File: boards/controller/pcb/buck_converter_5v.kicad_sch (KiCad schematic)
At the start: 10 parts, among them U801 LMR51430YFDDCR

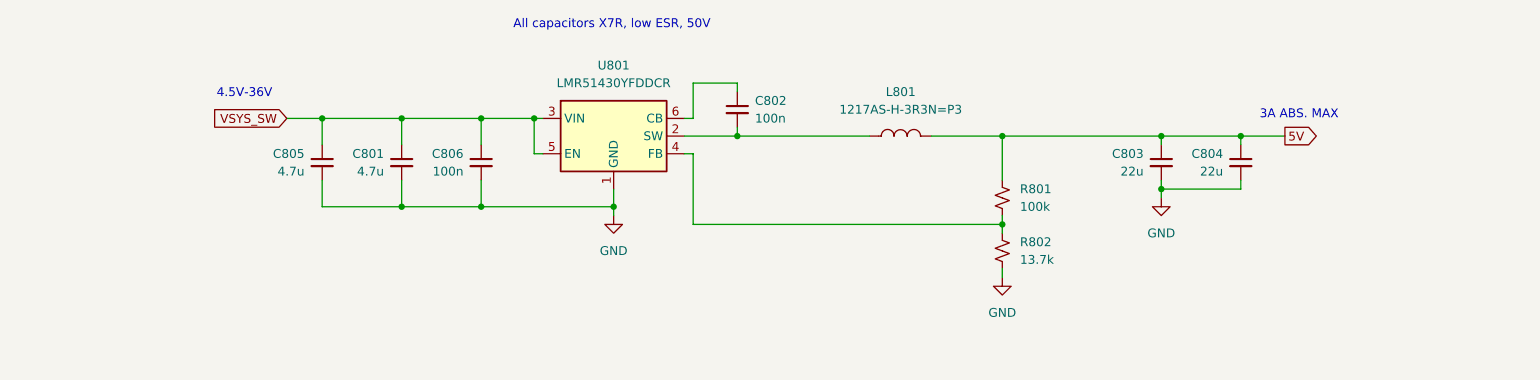
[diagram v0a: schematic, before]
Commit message: controller: pcb: Update schematic
Signed-off-by: Nicholas Loehrke <nicholasnloehrke@gmail.com>
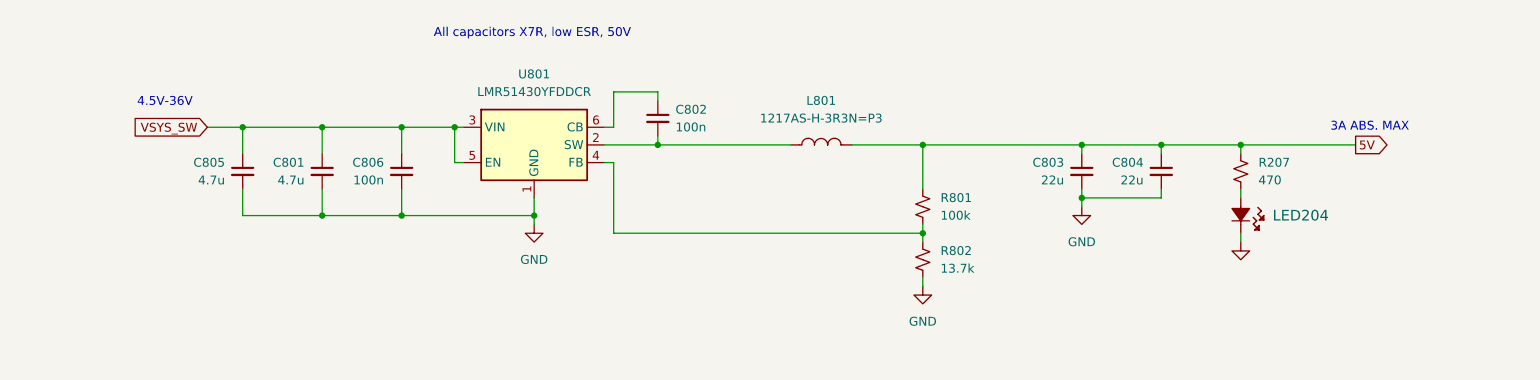
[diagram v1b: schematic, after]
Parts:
- added LED204: B1911PG--20D000514U1930, LED_B1911PG--20D000514U1930_HVK, symbol B1911PG--20D000514U1930:B1911PG--20D000514U1930
- added R207: 470, symbol Device:R_Small_US
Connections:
- net 5V: now also R207.1
- net GND: now also LED204.1
- new net: LED204.2, R207.2
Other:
- moved on the sheet: C801, C802, C803, C804, C805, C806, L801, R801, R802, U801

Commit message: controller: pcb: Update schematic
Signed-off-by: Nicholas Loehrke <nicholasnloehrke@gmail.com>
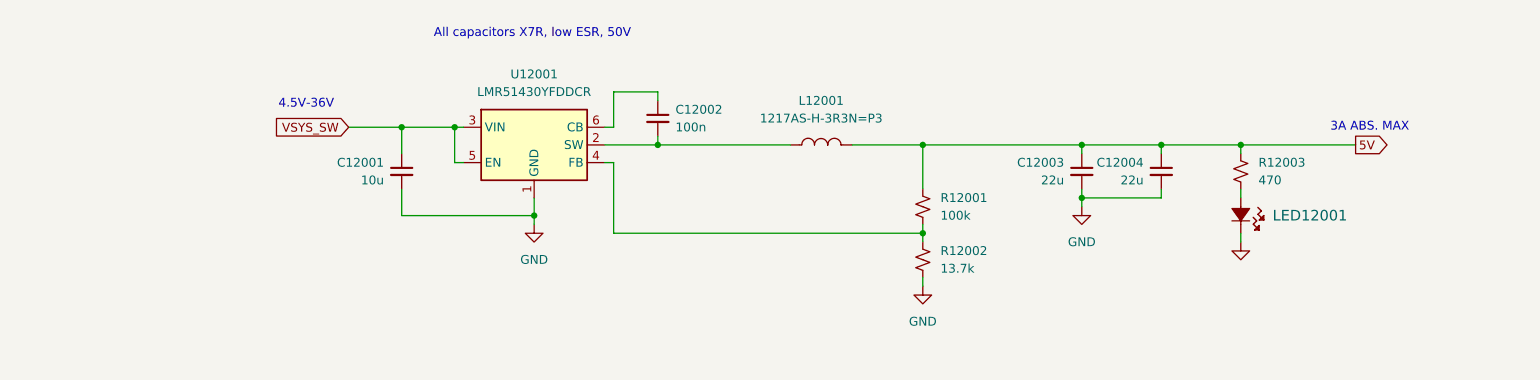
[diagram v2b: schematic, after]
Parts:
- removed C805: 4.7u, symbol Device:C_Small
- removed C806: 100n, symbol Device:C_Small
- C12001: renamed from C801; value 4.7u -> 10u
- renumbered C802 to C12002, C803 to C12003, C804 to C12004, L801 to L12001, LED204 to LED12001, R801 to R12001, R802 to R12002, R207 to R12003, U801 to U12001
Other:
- moved on the sheet: C12001

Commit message: controller: pcb: Update schematic
- Add power button pmos gate voltage clamp
- Add TVS diodes on encoders

Signed-off-by: Nicholas Loehrke <nicholasnloehrke@gmail.com>
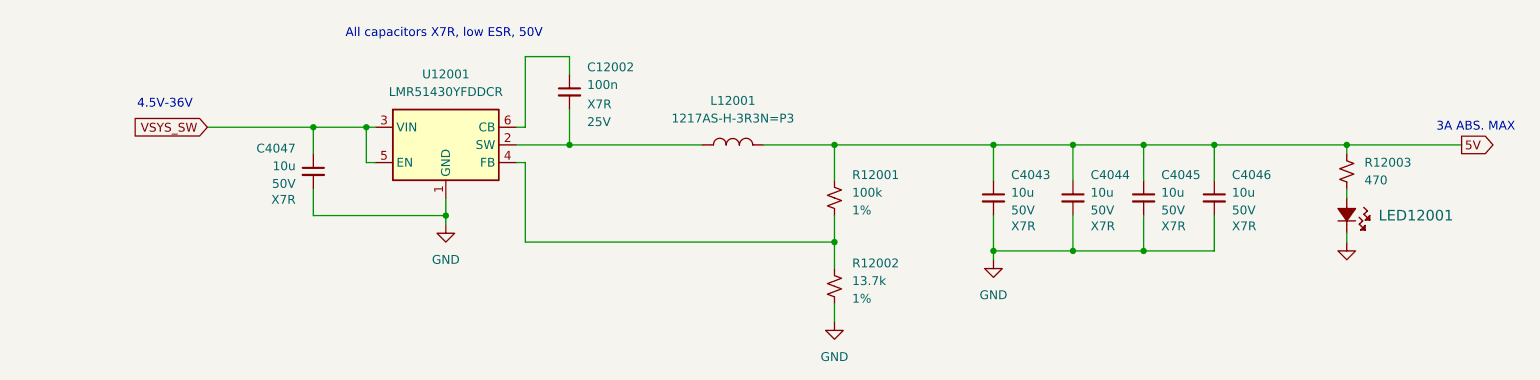
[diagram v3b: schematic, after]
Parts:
- removed C12001: 10u, symbol Device:C_Small
- removed C12003, C12004: 22u, symbol Device:C_Small
- added C4043, C4044, C4045, C4046, C4047: 10u, symbol Device:C_Small
- C12002: TCC (none) -> X7R; Voltage (none) -> 25V
- R12001, R12002: Tolerance (none) -> 1%
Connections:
- net 5V: now also C4043.1, C4044.1, C4045.1, C4046.1
- net GND: now also C4043.2, C4044.2, C4045.2, C4046.2, C4047.2
- net VSYS_SW: now also C4047.1
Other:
- moved on the sheet: C12002, L12001, LED12001, R12001, R12003, U12001

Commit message: controller: pcb: Update schematic
Signed-off-by: Nicholas Loehrke <nicholasnloehrke@gmail.com>
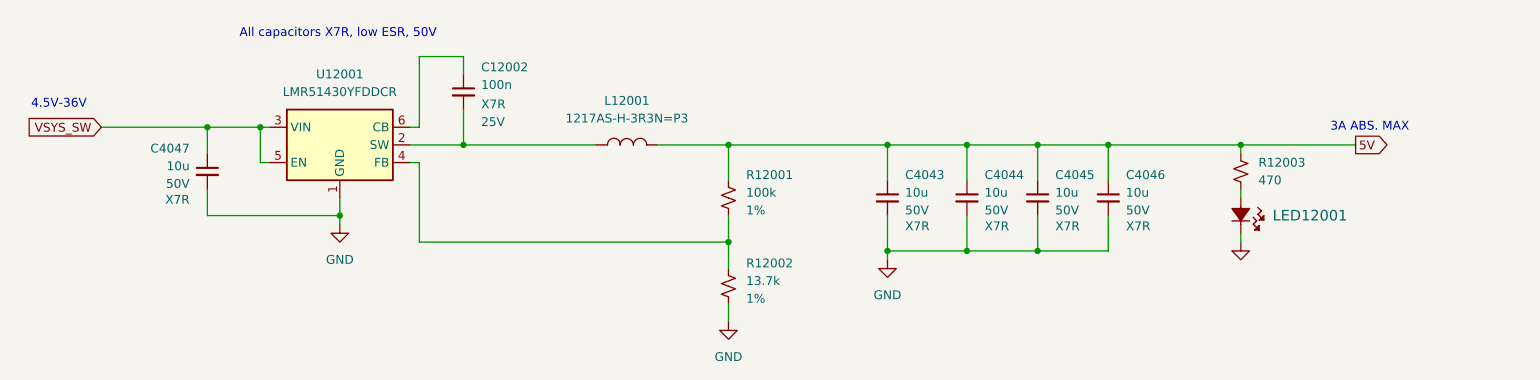
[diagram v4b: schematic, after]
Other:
- moved on the sheet: C12002, C4043, C4044, C4045, C4046, C4047, L12001, LED12001, R12001, R12002, R12003, U12001

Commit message: controller: pcb: Update schematic
Signed-off-by: Nicholas Loehrke <nicholasnloehrke@gmail.com>
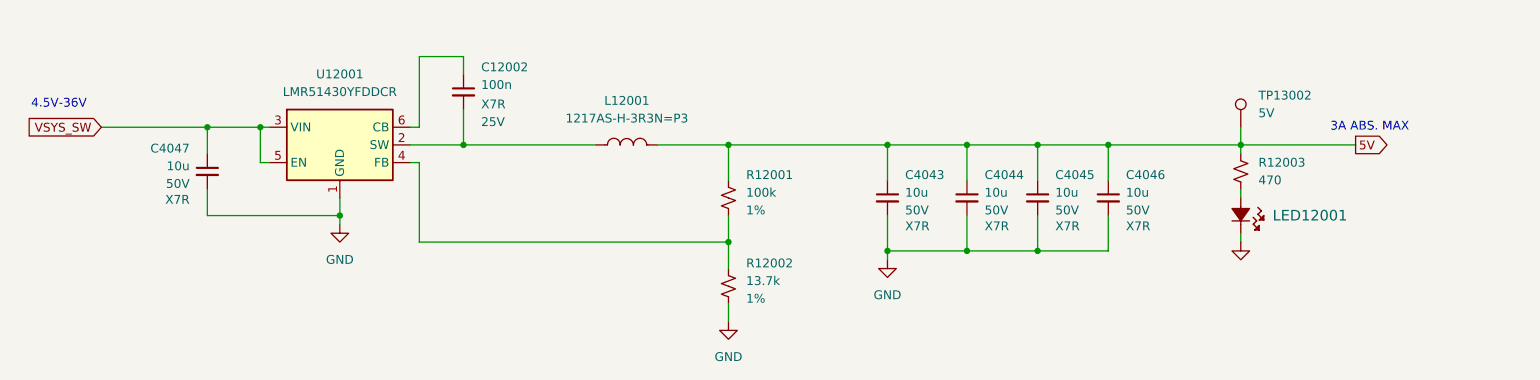
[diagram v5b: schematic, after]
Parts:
- added TP13002: 5V, symbol Connector:TestPoint
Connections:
- net 5V: now also TP13002.1
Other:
- note removed: "All capacitors X7R, low ESR, 50V"
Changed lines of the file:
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@@
 	(generator_version "9.0")
 	(paper "A4")
-	(text "All capacitors X7R, low ESR, 50V"
-		(exclude_from_sim no)
-		(at 96.266 83.058 0)
-		(effects
-			(font
-				(size 1.27 1.27)
-			)
-		)
-	)
 	(text "4.5V-36V"
 		(exclude_from_sim no)
@@
 		(pts
 			(xy 106.68 101.6) (xy 107.95 101.6)
+		)
+		(stroke
+			(width 0)
+			(type default)
+		)
+	)
+	(wire
+		(pts
+			(xy 226.06 96.52) (xy 226.06 99.06)
 		)
 		(stroke
@@
 					(unit 1)
 				)
+			)
+		)
+	)
+	(symbol
+		(lib_id "Connector:TestPoint")
+		(at 226.06 96.52 0)
+		(unit 1)
+		(exclude_from_sim no)
+		(in_bom yes)
+		(on_board yes)
+		(dnp no)
+		(fields_autoplaced yes)
+		(property "Reference" "TP13002"
+			(at 228.6 91.9479 0)
+			(effects
+				(font
+					(size 1.27 1.27)
+				)
+				(justify left)
+			)
+		)
+		(property "Value" "5V"
+			(at 228.6 94.4879 0)
+			(effects
+				(font
+					(size 1.27 1.27)
+				)
+				(justify left)
+			)
+		)
+		(property "Footprint" ""
+			(at 231.14 96.52 0)
+			(effects
+				(font
+					(size 1.27 1.27)
+				)
+				(hide yes)
+			)
+		)
+		(property "Datasheet" "~"
+			(at 231.14 96.52 0)
+			(effects
+				(font
+					(size 1.27 1.27)
+				)
+				(hide yes)
+			)
+		)
+		(property "Description" "test point"
+			(at 226.06 96.52 0)
+			(effects
+				(font
+					(size 1.27 1.27)
+				)
+				(hide yes)
+			)
+		)
+		(pin "1"
+		)
+		(instances
+			(project "controller"
+				(path "/5caba13a-97ae-46d4-856f-900b12012fd8/b034422d-7ead-4ba1-8965-68b1c7cd2df8"
+					(reference "TP13002")
+					(unit 1)
+				)

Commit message: controller: pcb: Update schematic + layout
Signed-off-by: Nicholas Loehrke <nicholasnloehrke@gmail.com>
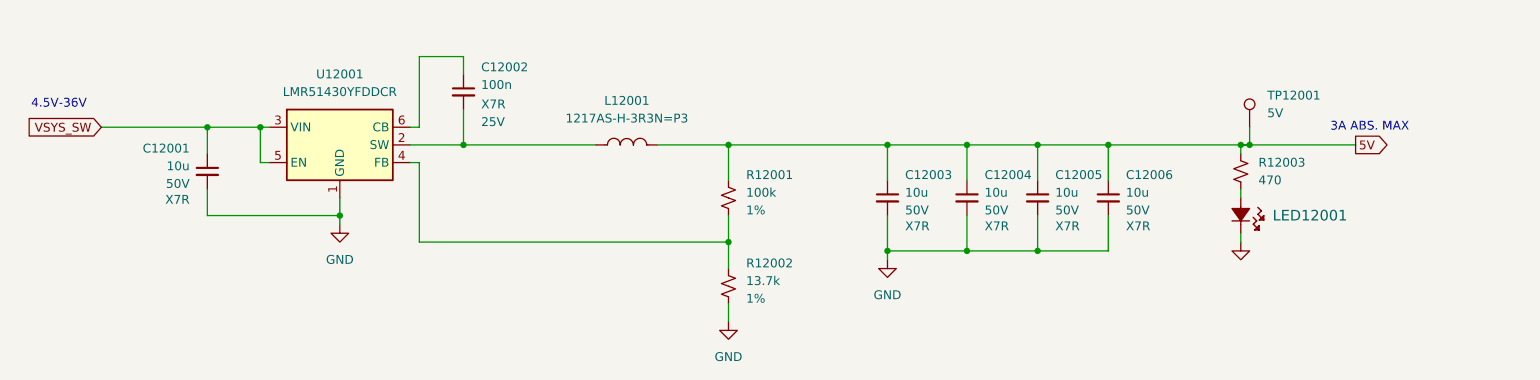
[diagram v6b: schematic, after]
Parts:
- C12001: renamed from C4047; footprint (none) -> Capacitor_SMD:C_1210_3225Metric
- C12002: footprint (none) -> Capacitor_SMD:C_0402_1005Metric
- C12003: renamed from C4043; footprint (none) -> Capacitor_SMD:C_1210_3225Metric
- C12004: renamed from C4044; footprint (none) -> Capacitor_SMD:C_1210_3225Metric
- C12005: renamed from C4045; footprint (none) -> Capacitor_SMD:C_1210_3225Metric
- C12006: renamed from C4046; footprint (none) -> Capacitor_SMD:C_1210_3225Metric
- L12001: footprint 1217AS-H-3R3N=P3:IND_1217AS-H-3R3N=P3 -> 1217AS-H-3R3N-P3:1217AS-H-3R3N-P3
- LED12001: footprint LED_B1911PG--20D000514U1930_HVK -> B1911PG--20D000514U1930:B1911PG--20D000514U1930
- R12001, R12002: footprint (none) -> Resistor_SMD:R_0402_1005Metric
- R12003: footprint (none) -> Resistor_SMD:R_0603_1608Metric
- TP12001: renamed from TP13002; footprint (none) -> TestPoint:TestPoint_Pad_D1.0mm
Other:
- moved on the sheet: TP12001
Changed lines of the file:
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@@
+	)
+	(junction
+		(at 227.33 99.06)
+		(diameter 0)
+		(color 0 0 0 0)
 	)
 	(junction
@@
 	(wire
 		(pts
-			(xy 226.06 96.52) (xy 226.06 99.06)
+			(xy 227.33 96.52) (xy 227.33 99.06)
 		)
 		(stroke
@@
 	(wire
 		(pts
+			(xy 227.33 99.06) (xy 226.06 99.06)
+		)
+		(stroke
+			(width 0)
+			(type default)
+		)
+	)
+	(wire
+		(pts
 			(xy 142.24 99.06) (xy 152.4 99.06)
 		)
@@
 	(wire
 		(pts
-			(xy 226.06 99.06) (xy 242.57 99.06)
+			(xy 226.06 99.06) (xy 227.33 99.06)
+		)
+		(stroke
+			(width 0.508)
+			(type default)
+		)
+	)
+	(wire
+		(pts
+			(xy 227.33 99.06) (xy 242.57 99.06)
 		)
 		(stroke
@@
 			)
 		)
-		(property "Footprint" ""
+		(property "Footprint" "Resistor_SMD:R_0603_1608Metric"
 			(at 226.06 102.87 0)
 			(effects
@@
 		(on_board yes)
 		(dnp no)
-		(property "Reference" "C4046"
+		(property "Reference" "C12006"
 			(at 209.55 103.378 0)
 			(effects
@@
 			)
 		)
-		(property "Footprint" ""
+		(property "Footprint" "Capacitor_SMD:C_1210_3225Metric"
 			(at 207.01 106.68 0)
 			(effects
@@
 			(project "controller"
 				(path "/5caba13a-97ae-46d4-856f-900b12012fd8/b034422d-7ead-4ba1-8965-68b1c7cd2df8"
-					(reference "C4046")
+					(reference "C12006")
 					(unit 1)
 				)
@@
 			)
 		)
-		(property "Footprint" ""
+		(property "Footprint" "Capacitor_SMD:C_0402_1005Metric"
 			(at 114.3 91.44 0)
 			(effects
@@
 	(symbol
 		(lib_id "Connector:TestPoint")
-		(at 226.06 96.52 0)
+		(at 227.33 96.52 0)
 		(unit 1)
 		(exclude_from_sim no)
@@
 		(dnp no)
 		(fields_autoplaced yes)
-		(property "Reference" "TP13002"
-			(at 228.6 91.9479 0)
+		(property "Reference" "TP12001"
+			(at 229.87 91.9479 0)
 			(effects
 				(font
@@
 		)
 		(property "Value" "5V"
-			(at 228.6 94.4879 0)
-			(effects
-				(font
-					(size 1.27 1.27)
-				)
-				(justify left)
-			)
-		)
-		(property "Footprint" ""
-			(at 231.14 96.52 0)
+			(at 229.87 94.4879 0)
+			(effects
+				(font
+					(size 1.27 1.27)
+				)
+				(justify left)
+			)
+		)
+		(property "Footprint" "TestPoint:TestPoint_Pad_D1.0mm"
+			(at 232.41 96.52 0)
 			(effects
 				(font
@@
 		)
 		(property "Datasheet" "~"
-			(at 231.14 96.52 0)
+			(at 232.41 96.52 0)
 			(effects
 				(font
@@
 		)
 		(property "Description" "test point"
-			(at 226.06 96.52 0)
+			(at 227.33 96.52 0)
 			(effects
 				(font
@@
 			(project "controller"
 				(path "/5caba13a-97ae-46d4-856f-900b12012fd8/b034422d-7ead-4ba1-8965-68b1c7cd2df8"
-					(reference "TP13002")
+					(reference "TP12001")
 					(unit 1)
 				)
@@
 		(on_board yes)
 		(dnp no)
-		(property "Reference" "C4045"
+		(property "Reference" "C12005"
 			(at 199.39 103.378 0)
 			(effects
@@
 			)
 		)
-		(property "Footprint" ""
+		(property "Footprint" "Capacitor_SMD:C_1210_3225Metric"
 			(at 196.85 106.68 0)
 			(effects
@@
 			(project "controller"
 				(path "/5caba13a-97ae-46d4-856f-900b12012fd8/b034422d-7ead-4ba1-8965-68b1c7cd2df8"
-					(reference "C4045")
+					(reference "C12005")
 					(unit 1)
 				)
@@
 		(on_board yes)
 		(dnp no)
-		(property "Reference" "C4043"
+		(property "Reference" "C12003"
 			(at 177.8 103.378 0)
 			(effects
@@
 			)
 		)
-		(property "Footprint" ""
+		(property "Footprint" "Capacitor_SMD:C_1210_3225Metric"
 			(at 175.26 106.68 0)
 			(effects
@@
 			(project "controller"
 				(path "/5caba13a-97ae-46d4-856f-900b12012fd8/b034422d-7ead-4ba1-8965-68b1c7cd2df8"
-					(reference "C4043")
+					(reference "C12003")
 					(unit 1)
 				)
@@
 			)
 		)
-		(property "Footprint" "LED_B1911PG--20D000514U1930_HVK"
+		(property "Footprint" "B1911PG--20D000514U1930:B1911PG--20D000514U1930"
 			(at 236.474 109.474 0)
 			(effects
@@
 		(on_board yes)
 		(dnp no)
-		(property "Reference" "C4047"
+		(property "Reference" "C12001"
 			(at 74.93 99.568 0)
 			(effects
@@
 			)
 		)
-		(property "Footprint" ""
+		(property "Footprint" "Capacitor_SMD:C_1210_3225Metric"
 			(at 77.47 102.87 0)
 			(effects
@@
 			(project "controller"
 				(path "/5caba13a-97ae-46d4-856f-900b12012fd8/b034422d-7ead-4ba1-8965-68b1c7cd2df8"
-					(reference "C4047")
+					(reference "C12001")
 					(unit 1)
 				)
@@
 		(on_board yes)
 		(dnp no)
-		(property "Reference" "C4044"
+		(property "Reference" "C12004"
 			(at 189.23 103.378 0)
 			(effects
@@
 			)
 		)
-		(property "Footprint" ""
+		(property "Footprint" "Capacitor_SMD:C_1210_3225Metric"
 			(at 186.69 106.68 0)
 			(effects
@@
 			(project "controller"
 				(path "/5caba13a-97ae-46d4-856f-900b12012fd8/b034422d-7ead-4ba1-8965-68b1c7cd2df8"
-					(reference "C4044")
+					(reference "C12004")
 					(unit 1)
 				)
@@
 			)
 		)
-		(property "Footprint" "1217AS-H-3R3N=P3:IND_1217AS-H-3R3N=P3"
+		(property "Footprint" "1217AS-H-3R3N-P3:1217AS-H-3R3N-P3"
 			(at 132.842 89.154 0)
 			(effects
@@
 			)
 		)
-		(property "Footprint" ""
+		(property "Footprint" "Resistor_SMD:R_0402_1005Metric"
 			(at 152.4 106.68 0)
 			(effects
@@
 			)
 		)
-		(property "Footprint" ""
+		(property "Footprint" "Resistor_SMD:R_0402_1005Metric"
 			(at 152.4 119.38 0)
 			(effects

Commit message: controller: Update BOM
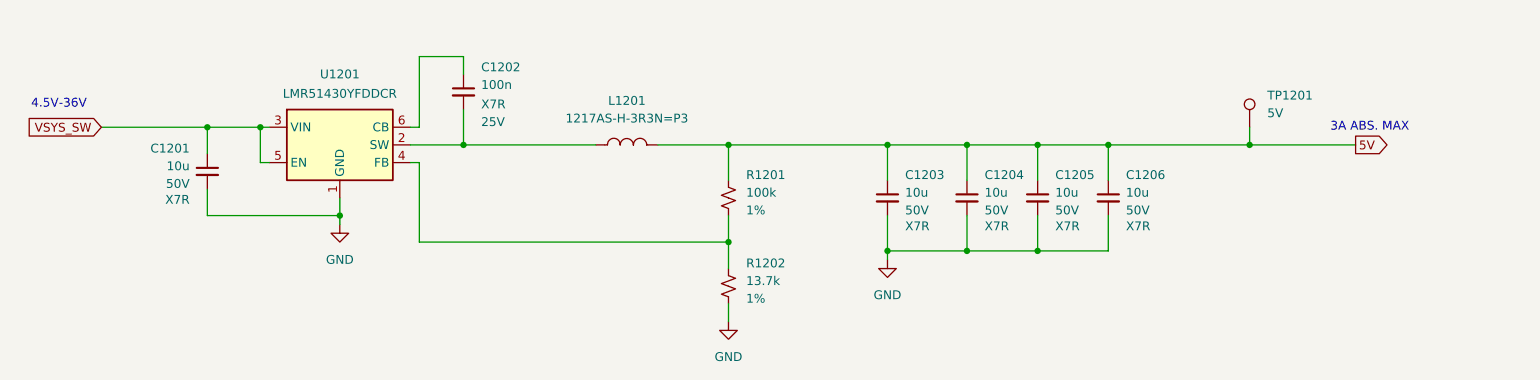
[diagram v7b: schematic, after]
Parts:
- removed LED12001: B1911PG--20D000514U1930, B1911PG--20D000514U1930:B1911PG--20D000514U1930, symbol B1911PG--20D000514U1930:B1911PG--20D000514U1930
- removed R12003: 470, Resistor_SMD:R_0603_1608Metric, symbol Device:R_Small_US
- L1201: renamed from L12001; MPN (none) -> 1217AS-H-3R3N=P3
- U1201: renamed from U12001; MPN (none) -> LMR51430YFDDCR
- renumbered C12001 to C1201, C12002 to C1202, C12003 to C1203, C12004 to C1204, C12005 to C1205, C12006 to C1206, R12001 to R1201, R12002 to R1202, TP12001 to TP1201
